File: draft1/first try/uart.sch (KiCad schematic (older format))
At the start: 0 parts

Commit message: labeled ft231xs-u
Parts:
- added C10, C11: LED, symbol Device:C
- added C12, C9: 47pF, symbol Device:C
- added C4, C5: 0.1uF, symbol Device:C
- added R3, R6: 27, symbol Device:R_US
- added R4: 270, symbol Device:R_US
- added U3: FT231XS-U, SOP64P599X175-20N, symbol SamacSys_Parts:FT231XS-U
- added U?: LP5907MFX-1.5, Package_TO_SOT_SMD:SOT-23-5, symbol Regulator_Linear:LP5907MFX-1.5
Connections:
- new net: C11.2, U3.10 (CBUS2)
- new net: R6.2, U3.11 (USBDP)
- new net: R3.1, U3.12 (USBDM)
- new net: C10.1, U3.17 (CBUS1)
- new net: C10.2, R4.2
- new net +UART33: C11.1, C4.1, C5.1, R4.1, U3.13 (3V3OUT), U3.14 (RESET#), U3.3 (VCCIO)
- new net +VUSB: U3.15 (VCC)
- new net D_N: C9.2, R3.2
- new net D_P: C12.1, R6.1
- new net GND: C12.2, C4.2, C5.2, C9.1, U3.16 (GND_2), U3.6 (GND_1)
- new net RsRx33: U3.20 (TXD)
- new net RsTx33: U3.4 (RXD)
- no-connect marks 0 -> 8

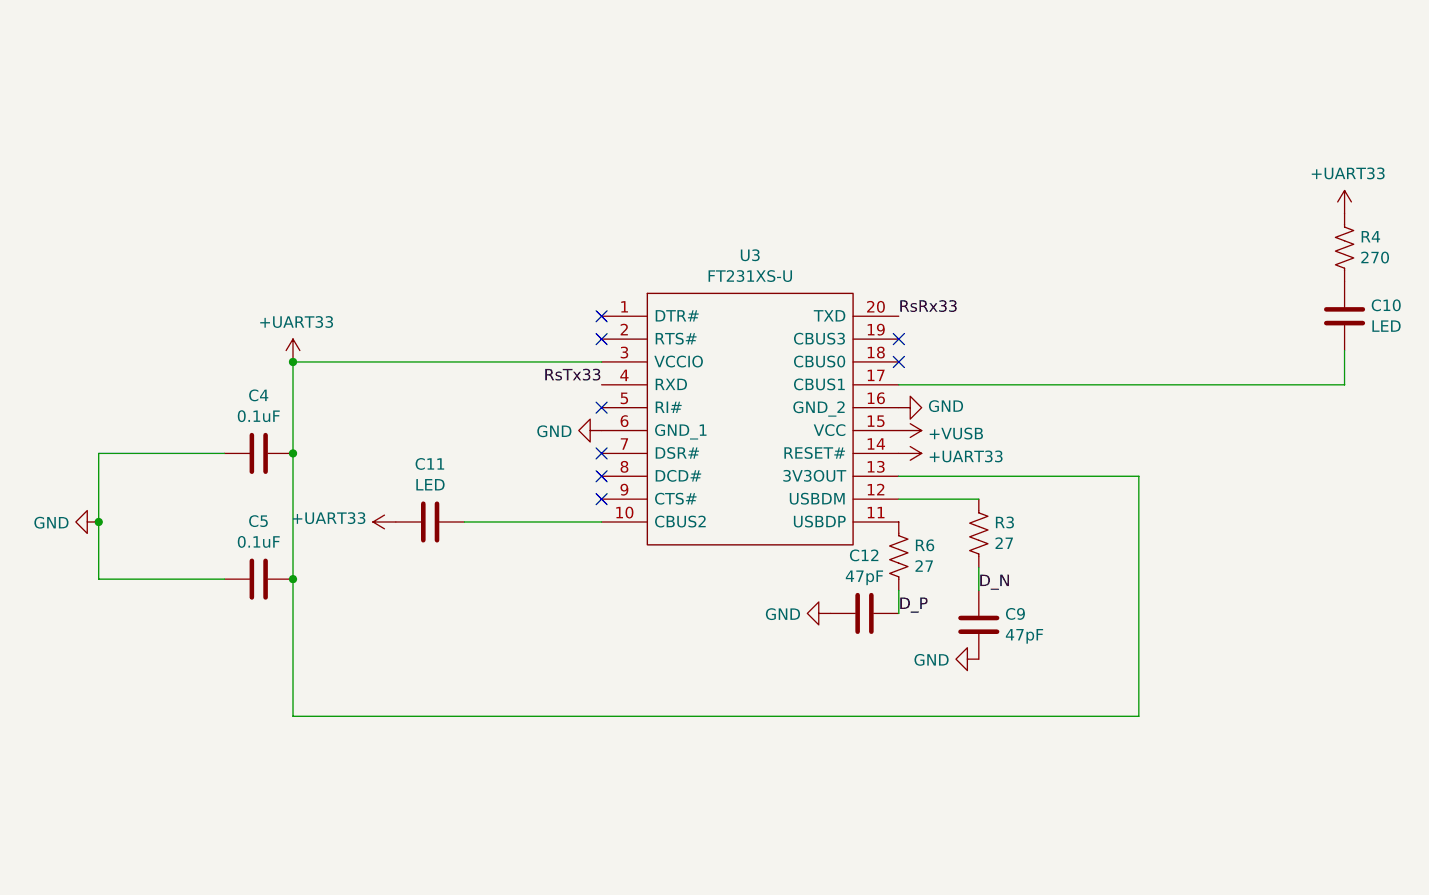
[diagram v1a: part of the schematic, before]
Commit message: added usb
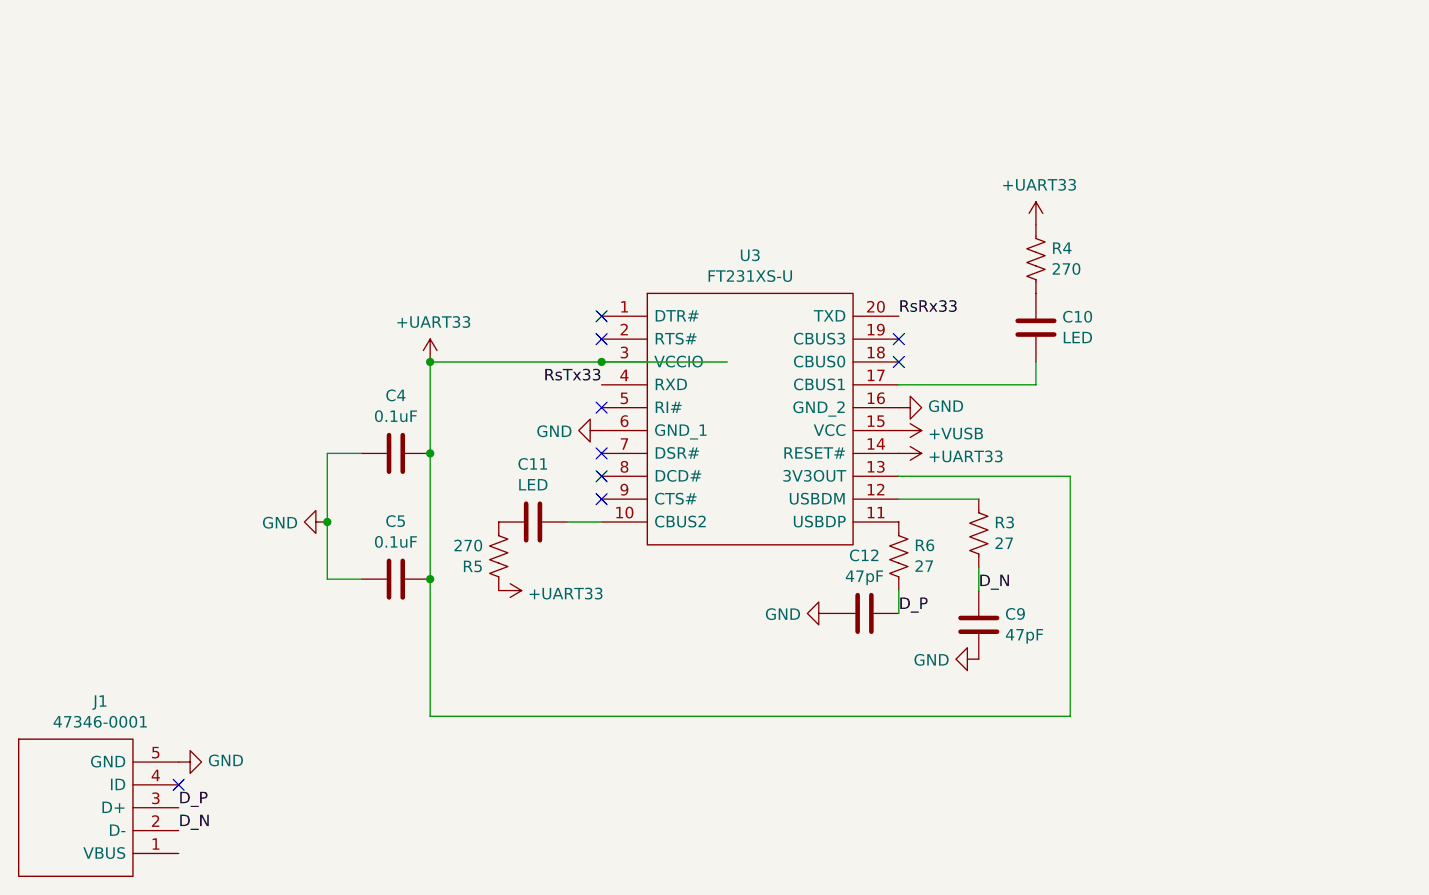
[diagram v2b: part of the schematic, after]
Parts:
- added J1: 47346-0001, 47346-0001, symbol SamacSys_Parts:47346-0001
- added R5: 270, symbol Device:R_US
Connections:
- wire segments 17 -> 18
- no-connect marks 8 -> 9
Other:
- moved on the sheet: C10, C11, C4, C5, R4
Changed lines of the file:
@@
 NoConn ~ 3450 4950
 Wire Wire Line
-	3450 5150 2100 5150
-$Comp
-L draft1library:+UART33 #PWR?
-U 1 1 5F3A0BD3
-P 2100 5150
-F 0 "#PWR?" H 2100 5000 50  0001 C CNN
-F 1 "+UART33" H 2115 5323 50  0000 C CNN
-F 2 "" H 2100 5150 50  0001 C CNN
-F 3 "" H 2100 5150 50  0001 C CNN
-	1    2100 5150
-	1    0    0    -1
-$EndComp
-Wire Wire Line
-	4750 5650 5800 5650
-Wire Wire Line
-	5800 5650 5800 6700
-Wire Wire Line
-	5800 6700 2100 6700
-Wire Wire Line
-	2100 6700 2100 6100
-Connection ~ 2100 5150
-$Comp
-L Device:C C4
-U 1 1 5F3A1B2E
-P 1950 5550
-F 0 "C4" V 1698 5550 50  0000 C CNN
-F 1 "0.1uF" V 1789 5550 50  0000 C CNN
-F 2 "" H 1988 5400 50  0001 C CNN
-F 3 "~" H 1950 5550 50  0001 C CNN
-	1    1950 5550
-	0    1    1    0
-$EndComp
-Connection ~ 2100 5550
-Wire Wire Line
-	2100 5550 2100 5150
-$Comp
-L Device:C C5
-U 1 1 5F3A35C7
-P 1950 6100
-F 0 "C5" V 1698 6100 50  0000 C CNN
-F 1 "0.1uF" V 1789 6100 50  0000 C CNN
-F 2 "" H 1988 5950 50  0001 C CNN
-F 3 "~" H 1950 6100 50  0001 C CNN
-	1    1950 6100
-	0    1    1    0
-$EndComp
-Connection ~ 2100 6100
-Wire Wire Line
-	2100 6100 2100 5550
-$Comp
-L power:GND #PWR?
-U 1 1 5F3A3C20
-P 1250 5850
-F 0 "#PWR?" H 1250 5600 50  0001 C CNN
-F 1 "GND" V 1255 5722 50  0000 R CNN
-F 2 "" H 1250 5850 50  0001 C CNN
-F 3 "" H 1250 5850 50  0001 C CNN
-	1    1250 5850
-	0    1    1    0
-$EndComp
-Wire Wire Line
-	1800 5550 1250 5550
-Wire Wire Line
-	1250 5550 1250 5850
-Wire Wire Line
-	1250 5850 1250 6100
-Wire Wire Line
-	1250 6100 1800 6100
-Connection ~ 1250 5850
+	4750 5650 5500 5650
 $Comp
 L draft1library:+VUSB #PWR?
@@
 L draft1library:+UART33 #PWR?
 U 1 1 5F3A76F2
-P 2550 5850
-F 0 "#PWR?" H 2550 5700 50  0001 C CNN
-F 1 "+UART33" V 2565 5978 50  0000 L CNN
-F 2 "" H 2550 5850 50  0001 C CNN
-F 3 "" H 2550 5850 50  0001 C CNN
-	1    2550 5850
-	0    -1   -1   0
+P 3000 6150
+F 0 "#PWR?" H 3000 6000 50  0001 C CNN
+F 1 "+UART33" V 3015 6278 50  0000 L CNN
+F 2 "" H 3000 6150 50  0001 C CNN
+F 3 "" H 3000 6150 50  0001 C CNN
+	1    3000 6150
+	0    1    1    0
 $EndComp
 $Comp
 L Device:C C11
 U 1 1 5F3A87B9
-P 2700 5850
-F 0 "C11" V 2952 5850 50  0000 C CNN
-F 1 "LED" V 2861 5850 50  0000 C CNN
-F 2 "" H 2738 5700 50  0001 C CNN
-F 3 "~" H 2700 5850 50  0001 C CNN
-	1    2700 5850
+P 3150 5850
+F 0 "C11" V 3402 5850 50  0000 C CNN
+F 1 "LED" V 3311 5850 50  0000 C CNN
+F 2 "" H 3188 5700 50  0001 C CNN
+F 3 "~" H 3150 5850 50  0001 C CNN
+	1    3150 5850
 	0    -1   -1   0
 $EndComp
 Wire Wire Line
-	2850 5850 3450 5850
+	3300 5850 3450 5850
 $Comp
 L Device:R_US R6
@@
 $EndComp
 Wire Wire Line
-	4750 5250 6700 5250
-Wire Wire Line
-	6700 5250 6700 5100
+	4750 5250 5350 5250
+Wire Wire Line
+	5350 5250 5350 5150
 $Comp
 L Device:C C10
 U 1 1 5F3BC9D0
-P 6700 4950
-F 0 "C10" H 6585 4904 50  0000 R CNN
-F 1 "LED" H 6585 4995 50  0000 R CNN
-F 2 "" H 6738 4800 50  0001 C CNN
-F 3 "~" H 6700 4950 50  0001 C CNN
-	1    6700 4950
+P 5350 5000
+F 0 "C10" H 5235 4954 50  0000 R CNN
+F 1 "LED" H 5235 5045 50  0000 R CNN
+F 2 "" H 5388 4850 50  0001 C CNN
+F 3 "~" H 5350 5000 50  0001 C CNN
+	1    5350 5000
 	-1   0    0    1
 $EndComp
@@
 L Device:R_US R4
 U 1 1 5F3BCF9F
-P 6700 4650
-F 0 "R4" H 6768 4696 50  0000 L CNN
-F 1 "270" H 6768 4605 50  0000 L CNN
-F 2 "" V 6740 4640 50  0001 C CNN
-F 3 "~" H 6700 4650 50  0001 C CNN
-	1    6700 4650
+P 5350 4700
+F 0 "R4" H 5418 4746 50  0000 L CNN
+F 1 "270" H 5418 4655 50  0000 L CNN
+F 2 "" V 5390 4690 50  0001 C CNN
+F 3 "~" H 5350 4700 50  0001 C CNN
+	1    5350 4700
 	1    0    0    -1
 $EndComp
@@
 L draft1library:+UART33 #PWR?
 U 1 1 5F3BDA8D
-P 6700 4500
-F 0 "#PWR?" H 6700 4350 50  0001 C CNN
-F 1 "+UART33" H 6715 4673 50  0000 C CNN
-F 2 "" H 6700 4500 50  0001 C CNN
-F 3 "" H 6700 4500 50  0001 C CNN
-	1    6700 4500
+P 5350 4550
+F 0 "#PWR?" H 5350 4400 50  0001 C CNN
+F 1 "+UART33" H 5365 4723 50  0000 C CNN
+F 2 "" H 5350 4550 50  0001 C CNN
+F 3 "" H 5350 4550 50  0001 C CNN
+	1    5350 4550
 	1    0    0    -1
 $EndComp
@@
 Text Label 4750 4950 0    50   ~ 0
 RsRx33
+Connection ~ 2250 5850
+Wire Wire Line
+	2250 6100 2400 6100
+Wire Wire Line
+	2250 5850 2250 6100
+Wire Wire Line
+	2250 5550 2250 5850
+Wire Wire Line
+	2400 5550 2250 5550
+$Comp
+L power:GND #PWR?
+U 1 1 5F3A3C20
+P 2250 5850
+F 0 "#PWR?" H 2250 5600 50  0001 C CNN
+F 1 "GND" V 2255 5722 50  0000 R CNN
+F 2 "" H 2250 5850 50  0001 C CNN
+F 3 "" H 2250 5850 50  0001 C CNN
+	1    2250 5850
+	0    1    1    0
+$EndComp
+Wire Wire Line
+	2700 6100 2700 5550
+Connection ~ 2700 6100
+$Comp
+L Device:C C5
+U 1 1 5F3A35C7
+P 2550 6100
+F 0 "C5" V 2298 6100 50  0000 C CNN
+F 1 "0.1uF" V 2389 6100 50  0000 C CNN
+F 2 "" H 2588 5950 50  0001 C CNN
+F 3 "~" H 2550 6100 50  0001 C CNN
+	1    2550 6100
+	0    1    1    0
+$EndComp
+Wire Wire Line
+	2700 5550 2700 5150
+Connection ~ 2700 5550
+$Comp
+L Device:C C4
+U 1 1 5F3A1B2E
+P 2550 5550
+F 0 "C4" V 2298 5550 50  0000 C CNN
+F 1 "0.1uF" V 2389 5550 50  0000 C CNN
+F 2 "" H 2588 5400 50  0001 C CNN
+F 3 "~" H 2550 5550 50  0001 C CNN
+	1    2550 5550
+	0    1    1    0
+$EndComp
+Wire Wire Line
+	2700 6700 2700 6100
+$Comp
+L draft1library:+UART33 #PWR?
+U 1 1 5F3A0BD3
+P 2700 5150
+F 0 "#PWR?" H 2700 5000 50  0001 C CNN
+F 1 "+UART33" H 2715 5323 50  0000 C CNN
+F 2 "" H 2700 5150 50  0001 C CNN
+F 3 "" H 2700 5150 50  0001 C CNN
+	1    2700 5150
+	1    0    0    -1
+$EndComp
+$Comp
+L Device:R_US R5
+U 1 1 5F3CE977
+P 3000 6000
+F 0 "R5" H 3068 6046 50  0000 L CNN
+F 1 "270" H 3068 5955 50  0000 L CNN
+F 2 "" V 3040 5990 50  0001 C CNN
+F 3 "~" H 3000 6000 50  0001 C CNN
+	1    3000 6000
+	-1   0    0    1
+$EndComp
+Wire Wire Line
+	5500 5650 5500 6700
+Wire Wire Line
+	3450 5150 4000 5150
+Wire Wire Line
+	5500 6700 2700 6700
+Wire Wire Line
+	2700 5150 3450 5150
+Connection ~ 2700 5150
+Connection ~ 3450 5150
+$Comp
+L SamacSys_Parts:47346-0001 J1
+U 1 1 5F3D9866
+P 1600 6900
+F 0 "J1" V 1335 7242 50  0000 C CNN
+F 1 "47346-0001" V 1426 7242 50  0000 C CNN
+F 2 "47346-0001" H 2150 7600 50  0001 L CNN
+F 3 "http://www.molex.com/pdm_docs/sd/473460001_sd.pdf" H 2150 7500 50  0001 L CNN
+F 4 "Micro USB B Receptacle Bottom Mount Assy Molex Right Angle SMT Type B Version 2.0 Micro USB Connector Socket, 30 V ac, 1A 47352 MICRO-USB" H 2150 7400 50  0001 L CNN "Description"
+F 5 "" H 2150 7300 50  0001 L CNN "Height"
+F 6 "Molex" H 2150 7200 50  0001 L CNN "Manufacturer_Name"
+F 7 "47346-0001" H 2150 7100 50  0001 L CNN "Manufacturer_Part_Number"
+F 8 "47346-0001" H 2150 7000 50  0001 L CNN "Arrow Part Number"
+F 9 "" H 2150 6900 50  0001 L CNN "Arrow Price/Stock"
+F 10 "538-47346-0001" H 2150 6800 50  0001 L CNN "Mouser Part Number"
+F 11 "https://www.mouser.co.uk/ProductDetail/Molex/47346-0001?qs=c2CV6XM0DweJBWaSeyWeCw%3D%3D" H 2150 6700 50  0001 L CNN "Mouser Price/Stock"
+	1    1600 6900
+	0    -1   1    0
+$EndComp
+$Comp
+L power:GND #PWR?
+U 1 1 5F3DD7AE
+P 1600 6900
+F 0 "#PWR?" H 1600 6650 50  0001 C CNN
+F 1 "GND" V 1605 6772 50  0000 R CNN
+F 2 "" H 1600 6900 50  0001 C CNN
+F 3 "" H 1600 6900 50  0001 C CNN
+	1    1600 6900
+	0    -1   -1   0
+$EndComp
+NoConn ~ 1600 7000
+Text Label 1600 7100 0    50   ~ 0
+D_P
+Text Label 1600 7200 0    50   ~ 0
+D_N
 $EndSCHEMATC

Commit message: added stuff
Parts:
- added C1, C3: 10uF, symbol Device:C
- added C2: NP, symbol Device:C
- added C6: 4.7uF, symbol Device:C
- added C7: 10nF, symbol Device:C
- added C8: 0.1uF, symbol Device:C
- added FB?: HZ0805E601R-10, BEADC2012X90N, symbol SamacSys_Parts:HZ0805E601R-10
- added IC? (x2): 74AVC1T45GS,132, 74LVC1G3157GS132, symbol SamacSys_Parts:74AVC1T45GS,132
- added R1, R2: NP, symbol Device:R_US
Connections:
- net labels added: +VBAT, +VDDIO, RsRx, RsTx
- wire segments 18 -> 46
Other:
- note added: "idk what goes here"
- moved on the sheet: J1
